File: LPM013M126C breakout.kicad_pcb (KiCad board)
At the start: 2 copper layers, 48.3 x 41.9 mm, 16 parts, among them J1 Conn_01x12

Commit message: change logo to library version
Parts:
- added REF**: Testudor-Logo_5mm_SilkScreen, Custom_Symbols:Testudor-Logo_5mm_SilkScreen, F.Cu at (168.9, 108.0)
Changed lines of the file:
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@@
       ) (layer "F.SilkS") (width 0.01) (fill solid))
+  )
+  (footprint "Custom_Symbols:Testudor-Logo_5mm_SilkScreen" (layer "F.Cu")
+    (at 168.91 107.95 90)
+    (fp_text reference "REF**" (at 0 -0.5 90 unlocked) (layer "F.SilkS") hide
+      (effects (font (size 1 1) (thickness 0.15)))
+    )
+    (fp_text value "Testudor-Logo_5mm_SilkScreen" (at 0 1 90 unlocked) (layer "F.Fab") hide
+      (effects (font (size 1 1) (thickness 0.15)))
+    )
+    (fp_poly (pts
+        (xy 1.744558 -1.12411)
+        (xy 1.308425 -0.872302)
+        (xy 1.744558 -1.560258)
+      ) (layer "F.SilkS") (width 0.000005) (fill solid))
+    (fp_poly (pts
+        (xy 0.872277 1.996366)
+        (xy 0.436144 2.248158)
+        (xy 0.872277 1.560171)
+      ) (layer "F.SilkS") (width 0.000005) (fill solid))
+    (fp_poly (pts
+        (xy 1.744558 -1.996391)
+        (xy 0.872277 -0.620509)
+        (xy -0.000005 0.755388)
+        (xy -0.000005 1.191475)
+        (xy 0.872277 -0.184361)
+        (xy 0.872277 0.251772)
+        (xy -0.000005 1.627669)
+        (xy -0.000005 2.063756)
+        (xy 0.872277 0.68792)
+        (xy 0.872277 1.124084)
+        (xy -0.000005 2.499951)
+        (xy -0.872286 1.996366)
+        (xy -0.872286 0.386708)
+        (xy -0.75542 0.31924)
+        (xy -0.000005 0.31924)
+        (xy 1.308425 -1.744599)
+        (xy 0.872277 -1.492791)
+        (xy -0.000005 -0.116893)
+        (xy -0.000005 0.31924)
+        (xy -0.75542 0.31924)
+        (xy -0.436138 0.134915)
+        (xy 0.436144 -1.240983)
+        (xy -0.000005 -0.989174)
+        (xy -0.872286 0.386708)
+        (xy -1.627694 -0.049426)
+        (xy -0.872286 -0.049426)
+        (xy -0.436138 -0.737366)
+        (xy -0.872286 -0.485558)
+        (xy -0.872286 -0.049426)
+        (xy -1.627694 -0.049426)
+        (xy -1.744552 -0.116893)
+        (xy -1.744552 -0.989174)
+        (xy 0.872277 -2.500008)
+      ) (layer "F.SilkS") (width 0.000005) (fill solid))
+    (group "" (id bfba5f06-7ce6-4059-b76a-a1d08e898bdb)
+      (members
+        3195c7bd-03c3-48d7-bb25-9324dd2c99c3
+        66df5a04-3007-4ad8-a45a-e564b25259f2
+        ece5223d-c903-40b3-b98a-5e16cbc2919f
+      )
+    )
   )
   (footprint "Custom_Display:LPM013M126C_silk" locked (layer "F.Cu")
@@
     )
   )
-  (gr_poly
-    (pts
-      (xy 171.655765 107.269996)
-      (xy 171.937208 107.757489)
-      (xy 171.168204 107.269996)
-    ) (layer "F.SilkS") (width 0.001) (fill solid))
-  (gr_poly
-    (pts
-      (xy 168.167821 106.294995)
-      (xy 168.449282 106.782488)
-      (xy 167.680311 106.294995)
-    ) (layer "F.SilkS") (width 0.001) (fill solid))
-  (gr_poly
-    (pts
-      (xy 167.192819 106.294995)
-      (xy 168.730726 107.269996)
-      (xy 170.26865 108.244998)
-      (xy 170.75609 108.244998)
-      (xy 169.218235 107.269996)
-      (xy 169.705727 107.269996)
-      (xy 171.243651 108.244998)
-      (xy 171.731091 108.244998)
-      (xy 170.193237 107.269996)
-      (xy 170.680763 107.269996)
-      (xy 172.218652 108.244998)
-      (xy 171.655765 109.22)
-      (xy 169.856553 109.22)
-      (xy 169.78114 109.089372)
-      (xy 169.78114 108.244998)
-      (xy 167.474263 106.782488)
-      (xy 167.755724 107.269996)
-      (xy 169.293648 108.244998)
-      (xy 169.78114 108.244998)
-      (xy 169.78114 109.089372)
-      (xy 169.575109 108.73249)
-      (xy 168.037185 107.757489)
-      (xy 168.318647 108.244998)
-      (xy 169.856553 109.22)
-      (xy 169.369061 110.064365)
-      (xy 169.369061 109.22)
-      (xy 168.600108 108.73249)
-      (xy 168.881569 109.22)
-      (xy 169.369061 109.22)
-      (xy 169.369061 110.064365)
-      (xy 169.293648 110.194984)
-      (xy 168.318647 110.194984)
-      (xy 166.629897 107.269996)
-    ) (layer "F.SilkS") (width 0.001) (fill solid))
   (gr_arc (start 127 80.01) (mid 128.115923 77.315923) (end 130.81 76.2) (layer "Edge.Cuts") (width 0.15))
   (gr_line (start 175.26 80.01) (end 175.26 114.3) (layer "Edge.Cuts") (width 0.15))
@@
     )
   )
-  (group "" (id 4fceaf1f-37d3-46c2-a6ca-fc3d15a43479)
-    (members
-      2d610706-7071-4a0f-9ff2-ad471173c947
-      407aecfb-365e-4346-9ac5-b0f8077cb126
-      b24af103-2914-4beb-921c-fa6871f8a89d
-    )
-  )

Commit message: fix references for R1, R2
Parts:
- R1: renamed from 21Ω1; value R1 -> 21Ω1
- R2: renamed from 21Ω2; value R2 -> 21Ω2
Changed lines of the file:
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@@
   (net 10 "EXTMODE")
   (net 11 "BL_C")
-  (net 12 "Net-(21Ω1-Pad2)")
-  (net 13 "Net-(21Ω2-Pad2)")
+  (net 12 "Net-(R1-Pad2)")
+  (net 13 "Net-(R2-Pad2)")
   (net 14 "BL_A")
   (footprint "MountingHole:MountingHole_3.2mm_M3_ISO14580_Pad_TopBottom" (layer "F.Cu")
@@
     (property "Sheetname" "")
     (attr smd)
-    (fp_text reference "21Ω1" (at 0 1.17 90) (layer "B.SilkS")
+    (fp_text reference "R1" (at 0 1.17 90) (layer "B.SilkS")
       (effects (font (size 1 1) (thickness 0.15)) (justify mirror))
     )
-    (fp_text value "R1" (at 0 -1.17 90) (layer "B.Fab")
+    (fp_text value "21Ω1" (at 0 -1.17 90) (layer "B.Fab")
       (effects (font (size 1 1) (thickness 0.15)) (justify mirror))
     )
@@
       (net 11 "BL_C") (pintype "passive"))
     (pad "2" smd roundrect (at 0.51 0 270) (size 0.54 0.64) (layers "B.Cu" "B.Paste" "B.Mask") (roundrect_rratio 0.25)
-      (net 12 "Net-(21Ω1-Pad2)") (pintype "passive"))
+      (net 12 "Net-(R1-Pad2)") (pintype "passive"))
     (model "${KICAD6_3DMODEL_DIR}/Resistor_SMD.3dshapes/R_0402_1005Metric.wrl"
       (offset (xyz 0 0 0))
@@
     (fp_line (start 1.85 0) (end 1.85 -3.6) (layer "B.Fab") (width 0.2))
     (pad "1" smd rect locked (at -0.75 -0.3 180) (size 0.3 0.7) (layers "B.Cu" "B.Paste" "B.Mask")
-      (net 12 "Net-(21Ω1-Pad2)") (pinfunction "Cathode2") (pintype "power_in"))
+      (net 12 "Net-(R1-Pad2)") (pinfunction "Cathode2") (pintype "power_in"))
     (pad "2" smd rect locked (at -0.25 -0.3 180) (size 0.3 0.7) (layers "B.Cu" "B.Paste" "B.Mask")
-      (net 13 "Net-(21Ω2-Pad2)") (pinfunction "Cathode1") (pintype "power_in"))
+      (net 13 "Net-(R2-Pad2)") (pinfunction "Cathode1") (pintype "power_in"))
     (pad "3" smd rect locked (at 0.25 -0.3 180) (size 0.3 0.7) (layers "B.Cu" "B.Paste" "B.Mask")
       (net 14 "BL_A") (pinfunction "Anode") (pintype "power_in"))
@@
     (property "Sheetname" "")
     (attr smd)
-    (fp_text reference "21Ω2" (at 0 1.17 90) (layer "B.SilkS")
+    (fp_text reference "R2" (at 0 1.17 90) (layer "B.SilkS")
       (effects (font (size 1 1) (thickness 0.15)) (justify mirror))
     )
-    (fp_text value "R2" (at 0 -1.17 90) (layer "B.Fab")
+    (fp_text value "21Ω2" (at 0 -1.17 90) (layer "B.Fab")
       (effects (font (size 1 1) (thickness 0.15)) (justify mirror))
     )
@@
       (net 11 "BL_C") (pintype "passive"))
     (pad "2" smd roundrect (at 0.51 0 270) (size 0.54 0.64) (layers "B.Cu" "B.Paste" "B.Mask") (roundrect_rratio 0.25)
-      (net 13 "Net-(21Ω2-Pad2)") (pintype "passive"))
+      (net 13 "Net-(R2-Pad2)") (pintype "passive"))
     (model "${KICAD6_3DMODEL_DIR}/Resistor_SMD.3dshapes/R_0402_1005Metric.wrl"
       (offset (xyz 0 0 0))

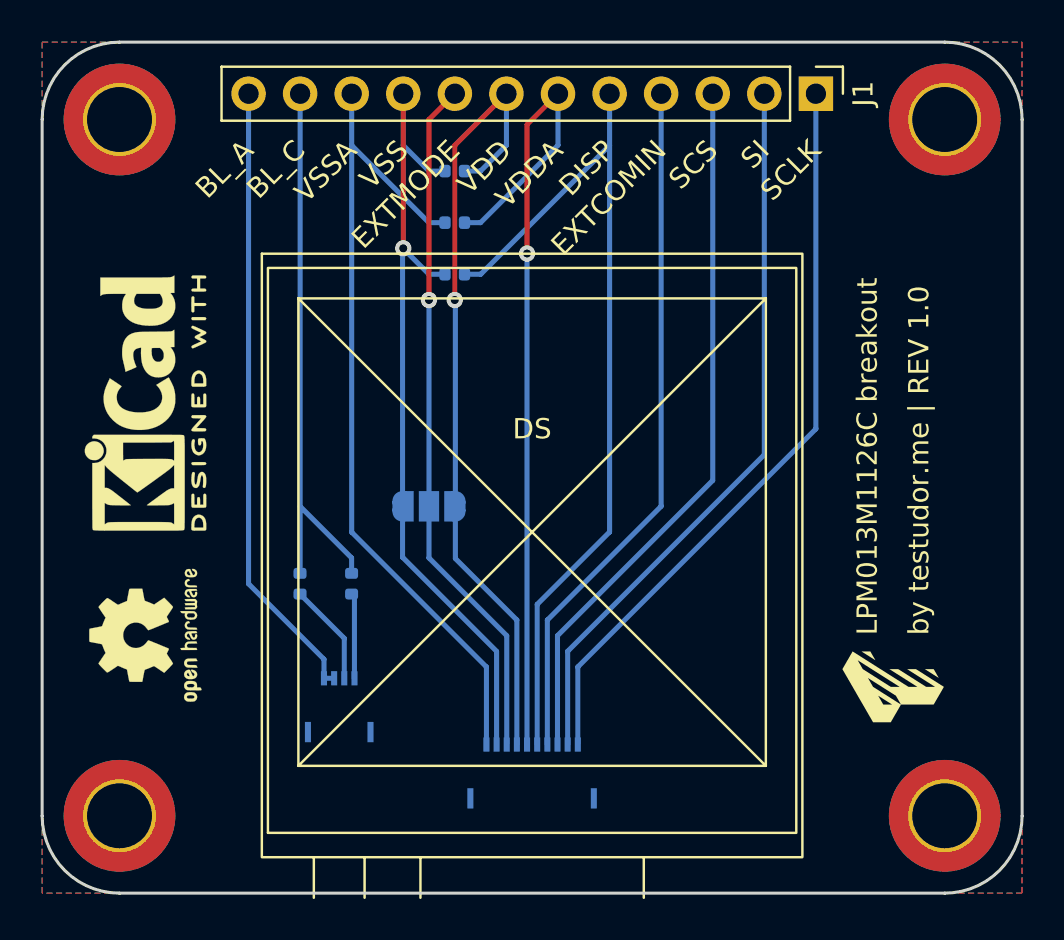
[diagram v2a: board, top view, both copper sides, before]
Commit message: Add BJT for backlight
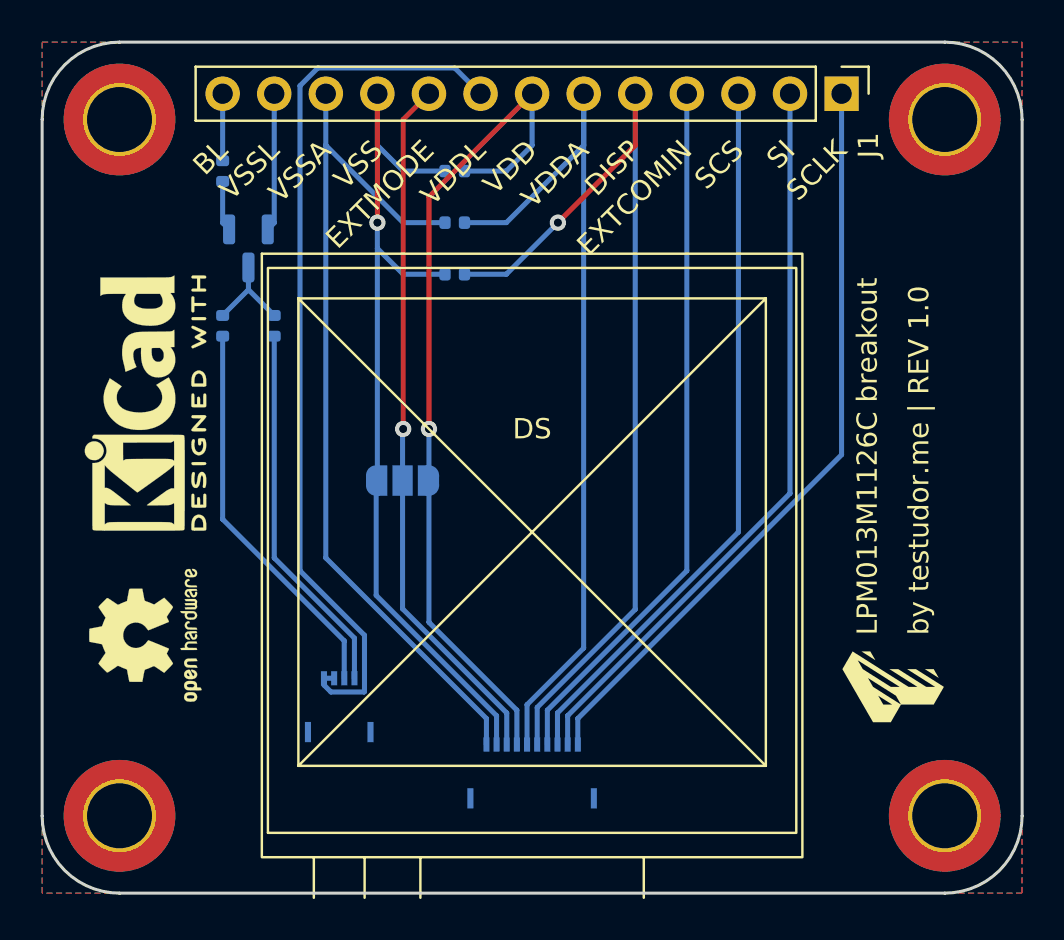
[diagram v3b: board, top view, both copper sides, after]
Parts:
- added Q1: MMBT2222ALT1G, Package_TO_SOT_SMD:SOT-23, B.Cu at (137.2, 86.4)
- added R3: 4k, Resistor_SMD:R_0402_1005Metric, B.Cu at (135.9, 82.5)
- J1: value Conn_01x12 -> Conn_01x13; footprint Connector_PinHeader_2.54mm:PinHeader_1x12_P2.54mm_Vertical -> Connector_PinHeader_2.54mm:PinHeader_1x13_P2.54mm_Vertical
- R1: value 21Ω1 -> 21
- R2: value 21Ω2 -> 21
- moved R1 13.3 mm to (138.4, 90.2)
- moved R2 13.3 mm to (135.9, 90.2)
- moved JP1 1.82 mm to (144.8, 97.8)
- moved J1 1.27 mm to (166.4, 78.7)
- renumbered REF** to MP1, REF** to MP2, REF** to MP3, REF** to MP4
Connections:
- DS2 pad 3: BL_A -> VDDL
- DS2 pad 4: BL_A -> VDDL
- J1 pad 10: VSSA -> VSS
- J1 pad 11: BL_C -> VSSA
- J1 pad 12: BL_A -> VSSL
- J1 pad 8: EXTMODE -> VDDL
- J1 pad 9: VSS -> EXTMODE
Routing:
- net VDDL: track 0.00 -> 43.9 mm
- net BL_A: track 30.8 -> 0.00 mm
- net BL_C: track 28.0 -> 4.68 mm
- net Net-(DS2-Pad2): track 5.05 -> 19.3 mm
- net Net-(DS2-Pad1): track 4.21 -> 18.5 mm
- net VSSL: track 0.00 -> 6.82 mm
- net DISP: track 43.3 -> 47.6 mm, vias 0 -> 1
- net BL: track 0.00 -> 3.30 mm
- net VSS: track 41.7 -> 44.8 mm
- net VDD: track 39.5 -> 42.3 mm
- net Net-(Q1-Pad1): track 0.00 -> 2.50 mm
- net VSSA: track 41.0 -> 42.8 mm
- net VDDA: track 41.4 -> 43.2 mm, vias 1 -> 0
- net EXTMODE: track 34.2 -> 34.7 mm
- net SI: track 36.1 -> 36.6 mm
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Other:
- board text added: "BL"
- board text added: "VDDL"
- board text added: "VSSL"
- board text removed: "BL_A"
- board text removed: "BL_C"

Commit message: add reference designators to logos
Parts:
- renumbered REF** to LOGO1, REF** to LOGO2, REF** to LOGO3
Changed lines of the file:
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@@
     (tags "Logo KiCad")
     (attr exclude_from_pos_files exclude_from_bom)
-    (fp_text reference "REF**" (at 0 -5.08 90) (layer "F.SilkS") hide
+    (fp_text reference "LOGO1" (at 0 -5.08 90) (layer "F.SilkS") hide
       (effects (font (size 1 1) (thickness 0.15)))
     )
@@
     (tags "Logo Symbol OSHW")
     (attr exclude_from_pos_files exclude_from_bom)
-    (fp_text reference "REF**" (at 0 0 90) (layer "F.SilkS") hide
+    (fp_text reference "LOGO2" (at 0 0 90) (layer "F.SilkS") hide
       (effects (font (size 1 1) (thickness 0.15)))
     )
@@
   (footprint "Custom_Symbols:Testudor-Logo_5mm_SilkScreen" (layer "F.Cu")
     (at 168.91 107.95 90)
-    (fp_text reference "REF**" (at 0 -0.5 90 unlocked) (layer "F.SilkS") hide
+    (fp_text reference "LOGO3" (at 0 -0.5 90 unlocked) (layer "F.SilkS") hide
       (effects (font (size 1 1) (thickness 0.15)))
     )

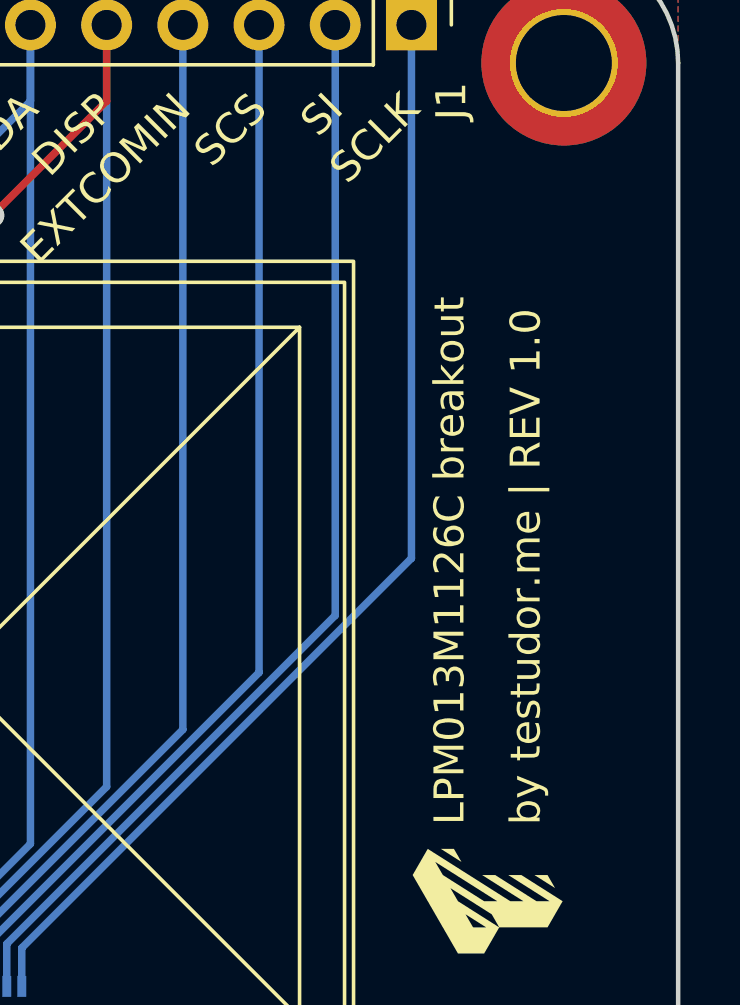
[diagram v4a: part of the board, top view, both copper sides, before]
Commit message: fix typo on PCB silkscreen
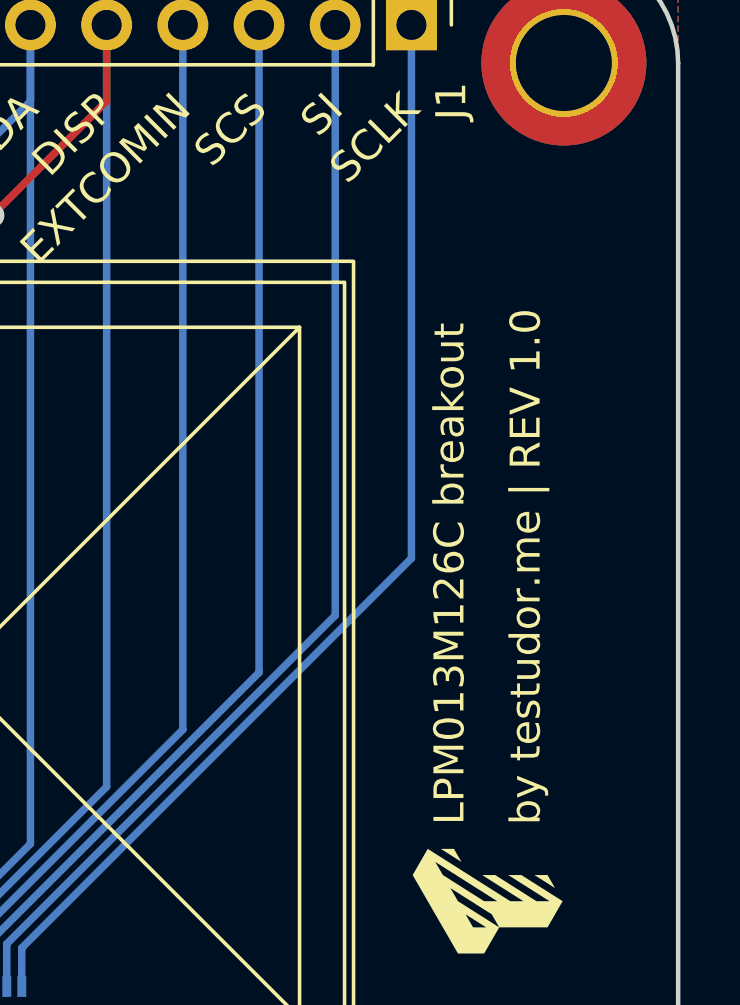
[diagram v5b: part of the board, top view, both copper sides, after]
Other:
- board text added: "LPM013M126C breakout"
- board text removed: "LPM013M1126C breakout"
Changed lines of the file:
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@@
     (effects (font (size 1 1) (thickness 0.15)) (justify left))
   )
-  (gr_text "LPM013M1126C breakout" (at 167.64 105.41 90) (layer "F.SilkS")
+  (gr_text "LPM013M126C breakout" (at 167.64 105.41 90) (layer "F.SilkS")
     (effects (font (size 1 1) (thickness 0.15)) (justify left))
   )

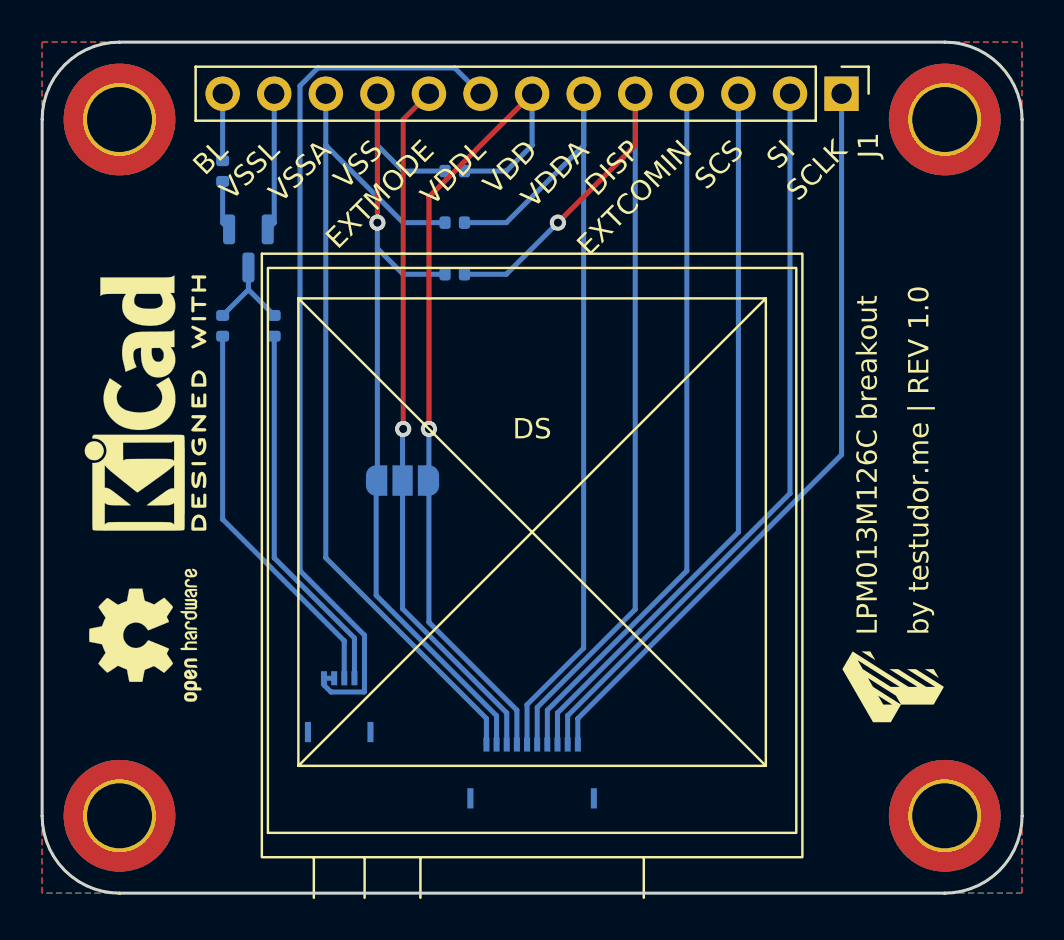
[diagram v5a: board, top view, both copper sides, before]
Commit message: modified pipeline to only run DRC and ERC checks
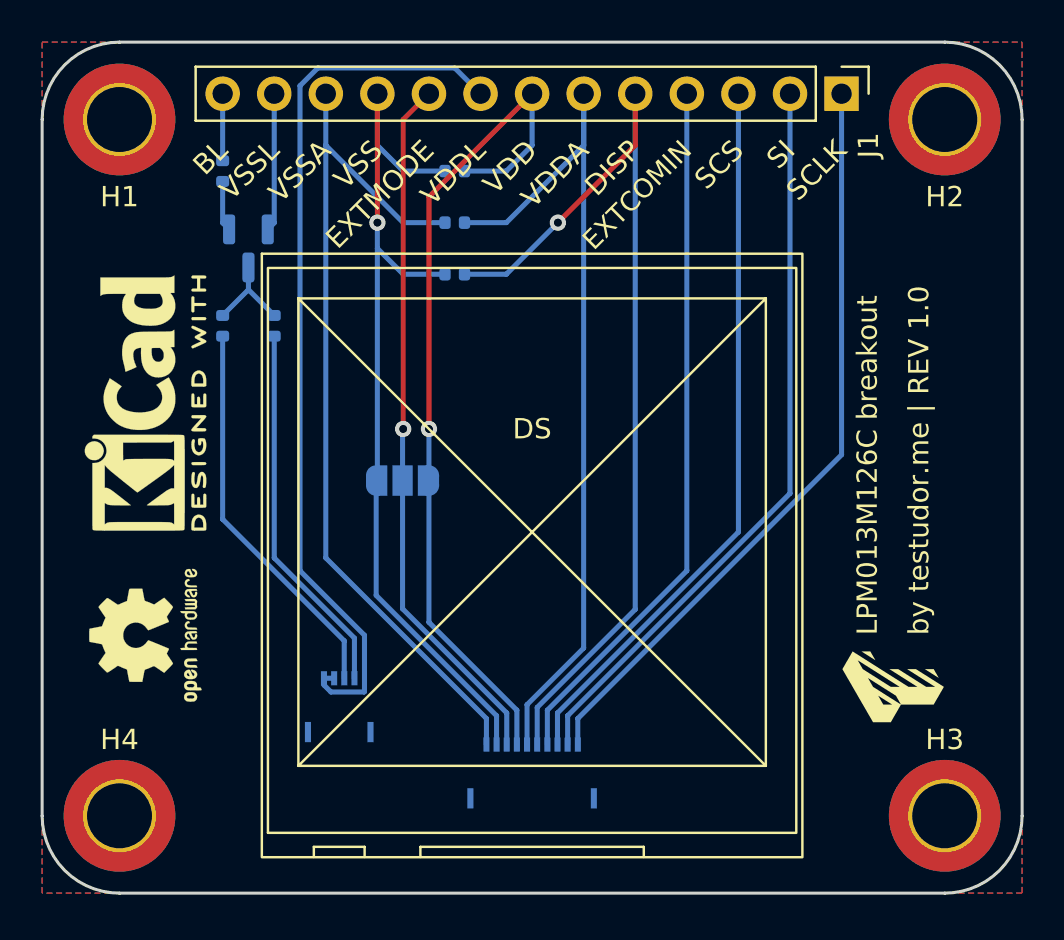
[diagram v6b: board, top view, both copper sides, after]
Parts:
- removed MP1, MP2, MP3, MP4: MountingHole_3.2mm_M3_ISO14580_Pad_TopBottom, MountingHole:MountingHole_3.2mm_M3_ISO14580_Pad_TopBottom
- added H1: MountingHole, MountingHole:MountingHole_3.2mm_M3_ISO14580_Pad_TopBottom, F.Cu at (130.8, 80.0)
- added H2: MountingHole, MountingHole:MountingHole_3.2mm_M3_ISO14580_Pad_TopBottom, F.Cu at (171.4, 80.0)
- added H3: MountingHole, MountingHole:MountingHole_3.2mm_M3_ISO14580_Pad_TopBottom, F.Cu at (171.4, 114.3)
- added H4: MountingHole, MountingHole:MountingHole_3.2mm_M3_ISO14580_Pad_TopBottom, F.Cu at (130.8, 114.3)
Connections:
- DS1 pad 11: (no net) -> unconnected-(DS1-Pad11)
- DS1 pad 12: (no net) -> unconnected-(DS1-Pad12)
- DS2 pad 5: (no net) -> unconnected-(DS2-Pad5)
- DS2 pad 6: (no net) -> unconnected-(DS2-Pad6)
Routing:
- added copper zone on B.Cu, net VDD
- added copper zone on F.Cu, net VDD
- removed copper zone on B.Cu, net (none)
- removed copper zone on F.Cu, net (none)
